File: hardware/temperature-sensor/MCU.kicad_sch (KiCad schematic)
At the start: 1 part, among them U1 STM32F407V_E-G_Tx

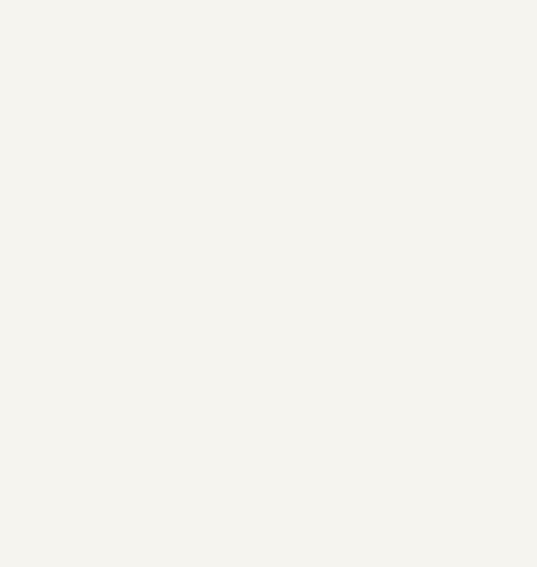
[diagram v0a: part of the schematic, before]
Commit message: add components for temperature sensor
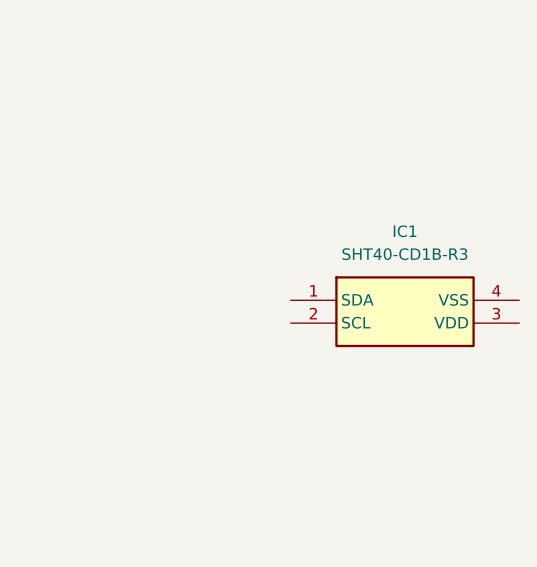
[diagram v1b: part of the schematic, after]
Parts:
- added IC1: SHT40-CD1B-R3, benediktibk:SHT40CD1BR3, symbol benediktibk:SHT40-CD1B-R3
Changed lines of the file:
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@@
 	(paper "A4")
+	(symbol
+		(lib_id "benediktibk:SHT40-CD1B-R3")
+		(at 201.93 81.28 0)
+		(unit 1)
+		(exclude_from_sim no)
+		(in_bom yes)
+		(on_board yes)
+		(dnp no)
+		(fields_autoplaced yes)
+		(property "Reference" "IC1"
+			(at 214.63 73.66 0)
+			(effects
+				(font
+					(size 1.27 1.27)
+				)
+			)
+		)
+		(property "Value" "SHT40-CD1B-R3"
+			(at 214.63 76.2 0)
+			(effects
+				(font
+					(size 1.27 1.27)
+				)
+			)
+		)
+		(property "Footprint" "benediktibk:SHT40CD1BR3"
+			(at 223.52 176.2 0)
+			(effects
+				(font
+					(size 1.27 1.27)
+				)
+				(justify left top)
+				(hide yes)
+			)
+		)
+		(property "Datasheet" "https://sensirion.com/media/documents/33FD6951/6555C40E/Sensirion_Datasheet_SHT4x.pdf"
+			(at 223.52 276.2 0)
+			(effects
+				(font
+					(size 1.27 1.27)
+				)
+				(justify left top)
+				(hide yes)
+			)
+		)
+		(property "Description" "Board Mount Humidity Sensors +/-1.8%RH/+/-0.2C, 4th generation, digital (I2C) humidity and temperature sensor with 0x46 I2C address."
+			(at 201.93 81.28 0)
+			(effects
+				(font
+					(size 1.27 1.27)
+				)
+				(hide yes)
+			)
+		)
+		(property "Height" "0.59"
+			(at 223.52 476.2 0)
+			(effects
+				(font
+					(size 1.27 1.27)
+				)
+				(justify left top)
+				(hide yes)
+			)
+		)
+		(property "Mouser Part Number" "403-SHT40-CD1B-R3"
+			(at 223.52 576.2 0)
+			(effects
+				(font
+					(size 1.27 1.27)
+				)
+				(justify left top)
+				(hide yes)
+			)
+		)
+		(property "Mouser Price/Stock" "https://www.mouser.co.uk/ProductDetail/Sensirion/SHT40-CD1B-R3?qs=ulEaXIWI0c%2FeyXO6eo5KrQ%3D%3D"
+			(at 223.52 676.2 0)
+			(effects
+				(font
+					(size 1.27 1.27)
+				)
+				(justify left top)
+				(hide yes)
+			)
+		)
+		(property "Manufacturer_Name" "Sensirion"
+			(at 223.52 776.2 0)
+			(effects
+				(font
+					(size 1.27 1.27)
+				)
+				(justify left top)
+				(hide yes)
+			)
+		)
+		(property "Manufacturer_Part_Number" "SHT40-CD1B-R3"
+			(at 223.52 876.2 0)
+			(effects
+				(font
+					(size 1.27 1.27)
+				)
+				(justify left top)
+				(hide yes)
+			)
+		)
+		(pin "1"
+		)
+		(pin "2"
+		)
+		(pin "3"
+		)
+		(pin "4"
+		)
+		(instances
+			(project ""
+				(path "/3594a937-0ff5-42e2-8a8f-f816088f7574/a0d45ccb-d615-45f4-a839-39b8e4e3dcc0"
+					(reference "IC1")
+					(unit 1)
+				)
+			)
+		)
+	)
 	(symbol
 		(lib_id "benediktibk:STM32F407V_E-G_Tx")

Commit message: extend schematic of ethernet
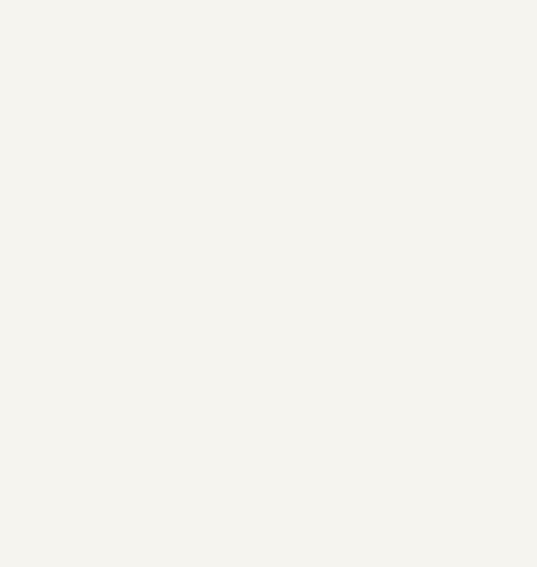
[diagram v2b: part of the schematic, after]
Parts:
- removed IC1: SHT40-CD1B-R3, benediktibk:SHT40CD1BR3, symbol benediktibk:SHT40-CD1B-R3
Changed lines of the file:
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@@
 	(paper "A4")
-	(symbol
-		(lib_id "benediktibk:SHT40-CD1B-R3")
-		(at 201.93 81.28 0)
-		(unit 1)
-		(exclude_from_sim no)
-		(in_bom yes)
-		(on_board yes)
-		(dnp no)
-		(fields_autoplaced yes)
-		(property "Reference" "IC1"
-			(at 214.63 73.66 0)
-			(effects
-				(font
-					(size 1.27 1.27)
-				)
-			)
-		)
-		(property "Value" "SHT40-CD1B-R3"
-			(at 214.63 76.2 0)
-			(effects
-				(font
-					(size 1.27 1.27)
-				)
-			)
-		)
-		(property "Footprint" "benediktibk:SHT40CD1BR3"
-			(at 223.52 176.2 0)
-			(effects
-				(font
-					(size 1.27 1.27)
-				)
-				(justify left top)
-				(hide yes)
-			)
-		)
-		(property "Datasheet" "https://sensirion.com/media/documents/33FD6951/6555C40E/Sensirion_Datasheet_SHT4x.pdf"
-			(at 223.52 276.2 0)
-			(effects
-				(font
-					(size 1.27 1.27)
-				)
-				(justify left top)
-				(hide yes)
-			)
-		)
-		(property "Description" "Board Mount Humidity Sensors +/-1.8%RH/+/-0.2C, 4th generation, digital (I2C) humidity and temperature sensor with 0x46 I2C address."
-			(at 201.93 81.28 0)
-			(effects
-				(font
-					(size 1.27 1.27)
-				)
-				(hide yes)
-			)
-		)
-		(property "Height" "0.59"
-			(at 223.52 476.2 0)
-			(effects
-				(font
-					(size 1.27 1.27)
-				)
-				(justify left top)
-				(hide yes)
-			)
-		)
-		(property "Mouser Part Number" "403-SHT40-CD1B-R3"
-			(at 223.52 576.2 0)
-			(effects
-				(font
-					(size 1.27 1.27)
-				)
-				(justify left top)
-				(hide yes)
-			)
-		)
-		(property "Mouser Price/Stock" "https://www.mouser.co.uk/ProductDetail/Sensirion/SHT40-CD1B-R3?qs=ulEaXIWI0c%2FeyXO6eo5KrQ%3D%3D"
-			(at 223.52 676.2 0)
-			(effects
-				(font
-					(size 1.27 1.27)
-				)
-				(justify left top)
-				(hide yes)
-			)
-		)
-		(property "Manufacturer_Name" "Sensirion"
-			(at 223.52 776.2 0)
-			(effects
-				(font
-					(size 1.27 1.27)
-				)
-				(justify left top)
-				(hide yes)
-			)
-		)
-		(property "Manufacturer_Part_Number" "SHT40-CD1B-R3"
-			(at 223.52 876.2 0)
-			(effects
-				(font
-					(size 1.27 1.27)
-				)
-				(justify left top)
-				(hide yes)
-			)
-		)
-		(pin "1"
-		)
-		(pin "2"
-		)
-		(pin "3"
-		)
-		(pin "4"
-		)
-		(instances
-			(project ""
-				(path "/3594a937-0ff5-42e2-8a8f-f816088f7574/a0d45ccb-d615-45f4-a839-39b8e4e3dcc0"
-					(reference "IC1")
-					(unit 1)
-				)
-			)
-		)
-	)
 	(symbol
 		(lib_id "benediktibk:STM32F407V_E-G_Tx")
